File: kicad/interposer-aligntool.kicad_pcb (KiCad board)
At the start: 2 copper layers, 47.1 x 47.1 mm, 1 part, among them U2 uPGA2

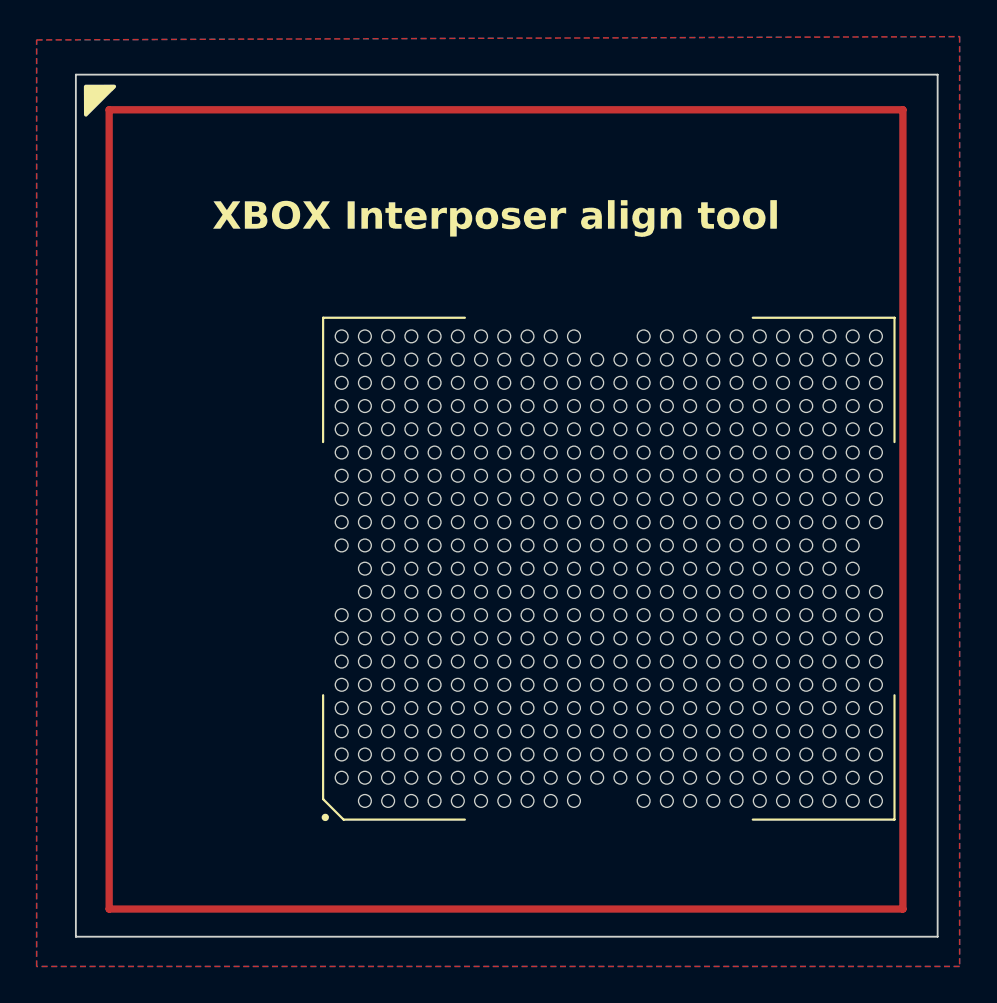
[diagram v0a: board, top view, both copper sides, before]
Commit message: Revision 3.2
Implement fixes that allow interposer to be actually functional for the first time:
 - Fix uBGA495 pin P1 from VTT --> VCC since this is VCC on xbox motherboard.
 - Fix P370 pin AJ3 (RESET2#) from GND --> NC.

Furthermore, pins AL1 (reserved), AK36 (VID output), AF36 (DETECT) now left NC instead of connected to GND.

Outline slightly trimmed near bottom to provide some clearance against a cap on 1.6 motherboards.

Design specs loosened, from 4 mil tracks/4 mil clearance/0.3mm drills --> 5 mil/5 mil/0.3mm.

Board thickness recommendation is now 1.6mm instead of 1.2mm for additional rigidity.
Trace lengths now matched at 27.0mm (was 25.0mm).

Added BGA footprint indicator on front silkscreen.
Added BGA pin numbering on back silkscreen.
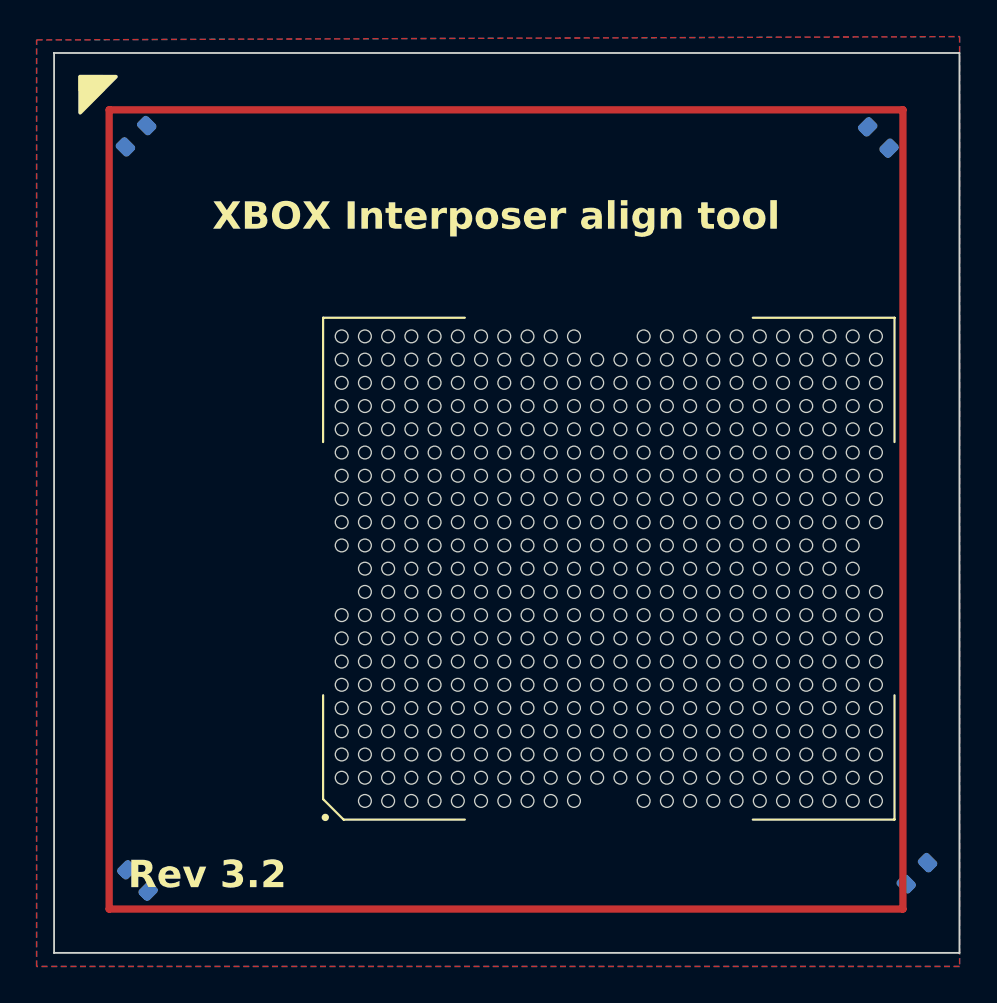
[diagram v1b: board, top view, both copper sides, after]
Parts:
- added ?: R_0603_1608Metric, Resistor_SMD:R_0603_1608Metric, B.Cu at (162.0, 76.7)
- added ?: R_0603_1608Metric, Resistor_SMD:R_0603_1608Metric, B.Cu at (164.1, 116.9)
- added ?: R_0603_1608Metric, Resistor_SMD:R_0603_1608Metric, B.Cu at (121.5, 117.3)
- added ?: R_0603_1608Metric, Resistor_SMD:R_0603_1608Metric, B.Cu at (121.5, 76.6)
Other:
- board size 47.1 x 47.1 mm -> 49.5 x 49.2 mm
- board text added: "Rev 3.2"

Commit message: Rev. 3.3, minor changes:  - Resistor network RN01 changed to 4 distinct 0603's since people continuously order an incorrect part  - Height of interposer slightly reduced by 0.3mm on both top and bottom. on top, the pins for standard mounting bracket require less trimming. On bottom there is less obstruction with C1D5 on xbox motherboard.  - Added xbox.munia.io branding on the bottom silk  - Align tool modified accordingly.
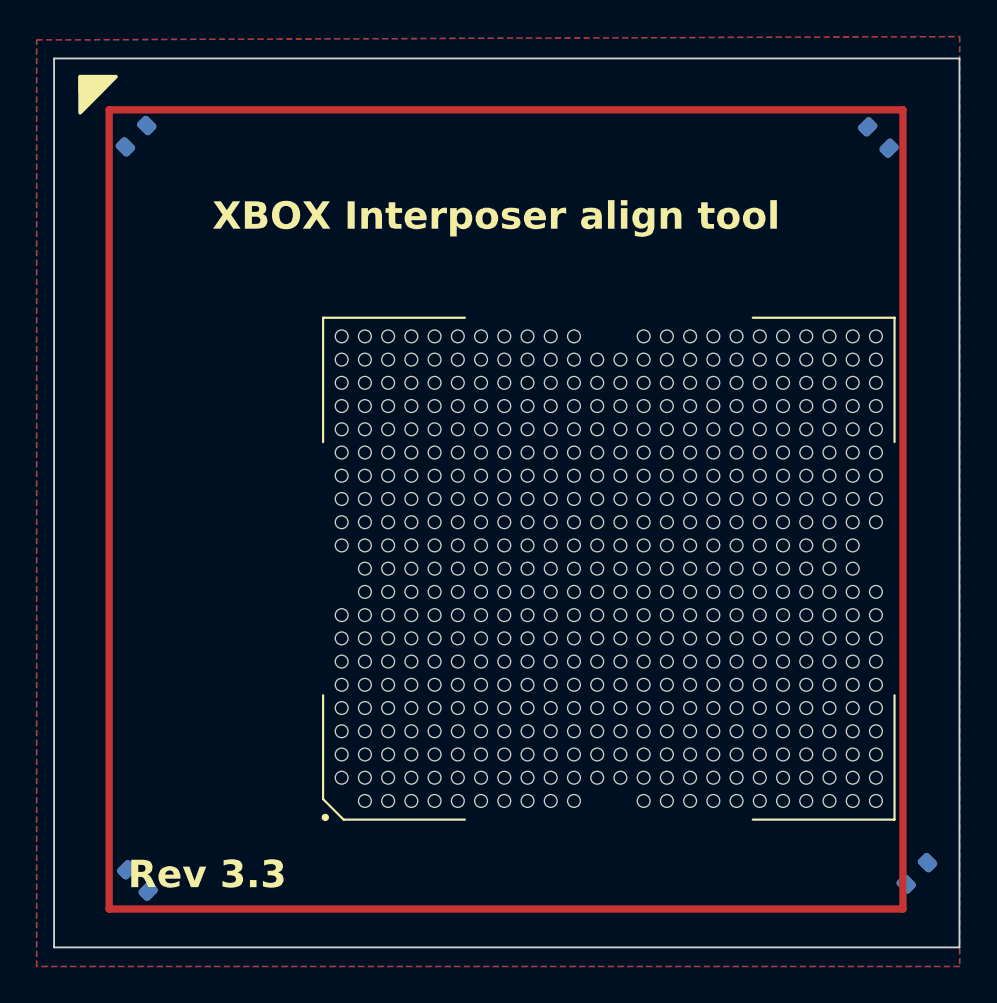
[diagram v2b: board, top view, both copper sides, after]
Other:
- board size 49.5 x 49.2 mm -> 49.5 x 48.6 mm
- board text added: "Rev 3.3"
- board text added: "http://xbox.munia.io"
- board text removed: "Rev 3.2"
